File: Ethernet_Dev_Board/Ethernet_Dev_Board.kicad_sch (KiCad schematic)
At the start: 27 parts, among them J101 Power In, J102 5V, J103 3.3V, J104 3.3VA, J105 3.3VD, U101 AZ1117

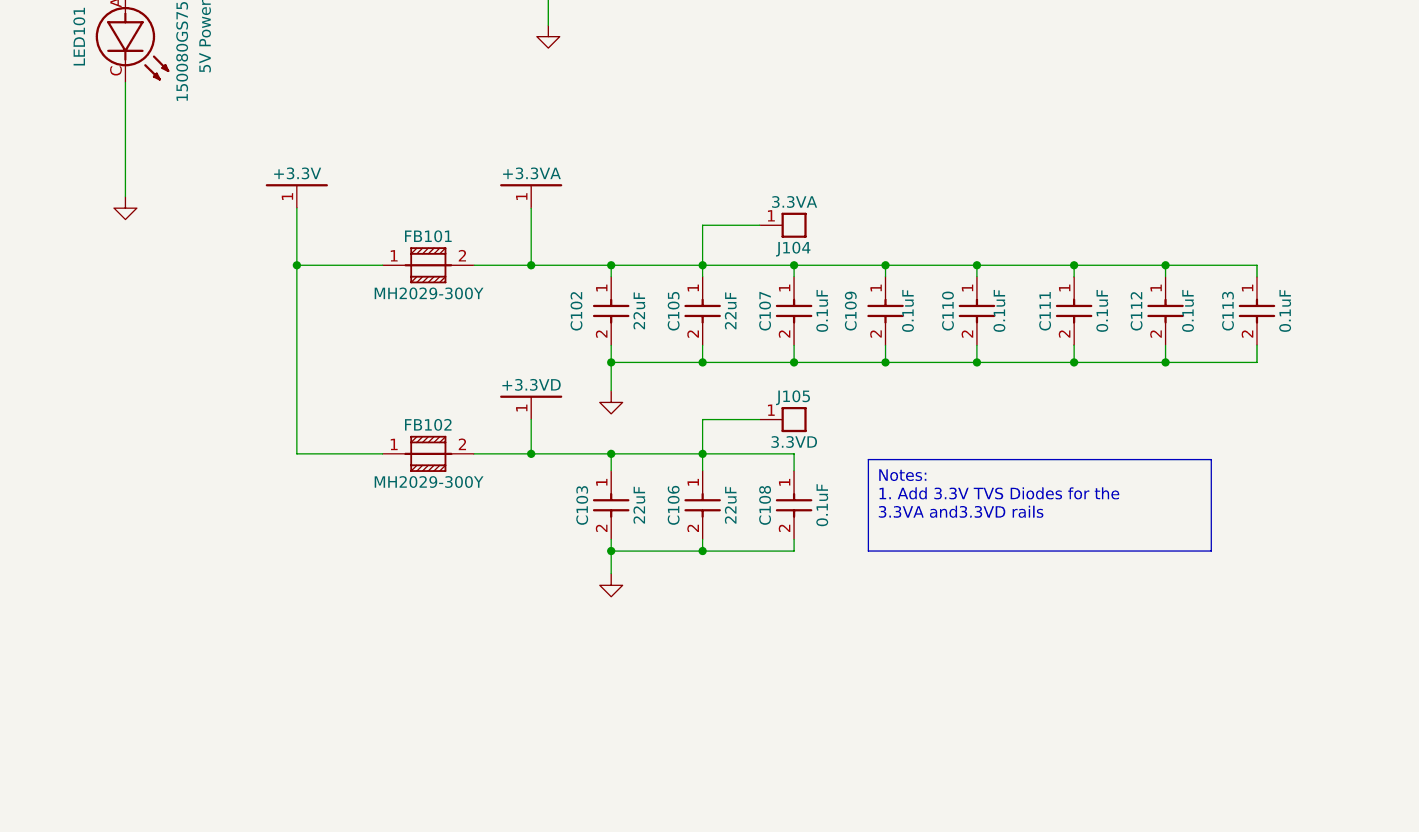
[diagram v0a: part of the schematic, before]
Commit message: Added TVS diode and redid the LED circuit on the ESP32
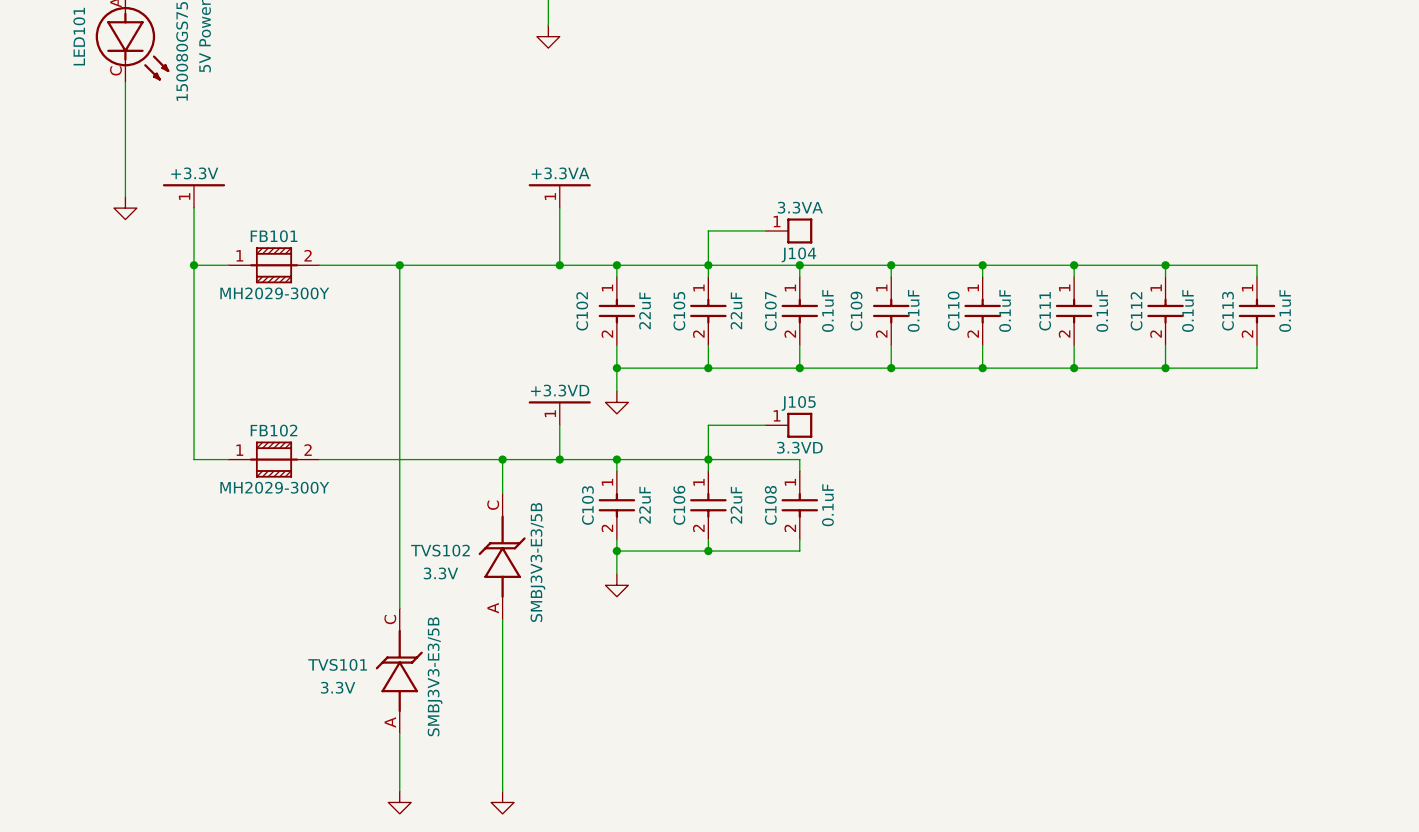
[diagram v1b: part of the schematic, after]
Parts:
- added TVS101, TVS102: 3.3V, RG_Diode:SMB-D, symbol RG_Diode:TVS
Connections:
- net +3.3VA: now also TVS101.C (2)
- net +3.3VD: now also TVS102.C (2)
- net GNDS: now also TVS101.A (1), TVS102.A (1)
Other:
- moved on the sheet: C102, C103, C105, C106, C107, C108, C109, C110, FB101, FB102, J104, J105

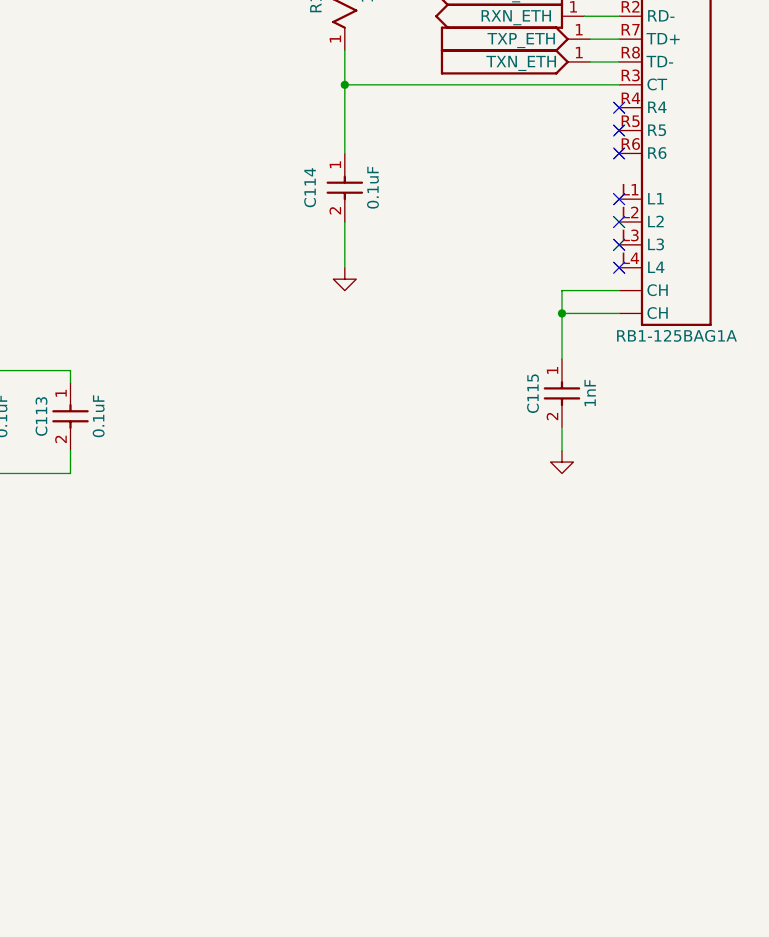
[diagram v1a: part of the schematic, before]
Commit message: Added in 1.2 V regulator and broke out unused IO pins to header
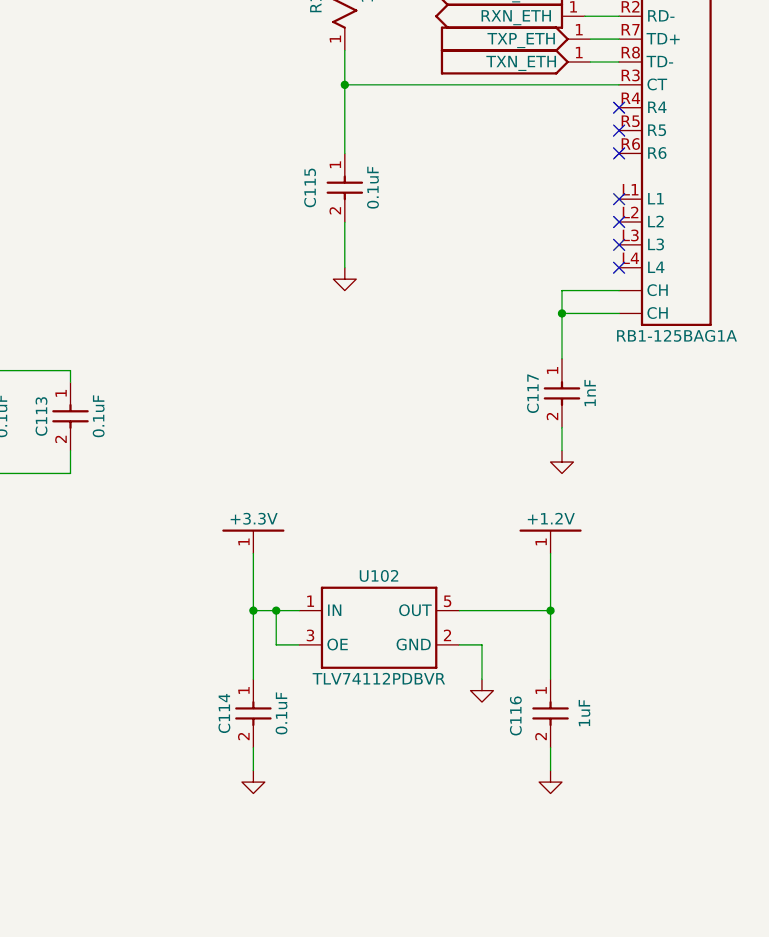
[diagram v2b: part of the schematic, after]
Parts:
- added C114: 0.1uF, RG_Capacitors_SMD:0603, symbol LED_Controller_Hardware-eagle-import:CAP-0603
- added C116: 1uF, RG_Capacitors_SMD:0603, symbol RG_Capacitors:CAP-0603
- added U102: 1.2V, RG_TO_SOT_SMD:SOT23-5P65, symbol RG_Regulators:TLV74112PDBVR
- renumbered C114 to C115, C115 to C117
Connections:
- net +3.3V: now also C114.1, U102.1 (IN), U102.3 (OE)
- net GNDS: now also C114.2, C116.2, U102.2 (GND)
- new net +1.2V: C116.1, U102.5 (OUT)

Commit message: Net adjustments. Beginning board layout
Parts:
- removed J102: 5V, RG_Terminals:PAD_0.0638, symbol LED_Controller_Hardware-eagle-import:5V
- removed J103: 3.3V, RG_Terminals:PAD_0.0638, symbol LED_Controller_Hardware-eagle-import:3.3V
- removed J104: 3.3VA, RG_Terminals:PAD_0.0638, symbol LED_Controller_Hardware-eagle-import:3.3VA
- removed J105: 3.3VD, RG_Terminals:PAD_0.0638, symbol LED_Controller_Hardware-eagle-import:3.3VD
- LED101: value 5V Power -> Power
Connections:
- net GND1: now also C102.2, C103.2, C105.2, C106.2, C107.2, C108.2, C109.2, C110.2, C111.2, C112.2, C113.2, C114.2, C115.2, C116.2, C117.2, TVS101.A (1), TVS102.A (1)
- net GNDS: no longer C102.2, C103.2, C105.2, C106.2, C107.2, C108.2, C109.2, C110.2, C111.2, C112.2, C113.2, C114.2, C115.2, C116.2, C117.2, TVS101.A (1), TVS102.A (1)
- net RXN_ETH renamed ETH_RX_N
- net RXP_ETH renamed ETH_RX_P
- net TXN_ETH renamed ETH_TX_N
- net TXP_ETH renamed ETH_TX_P

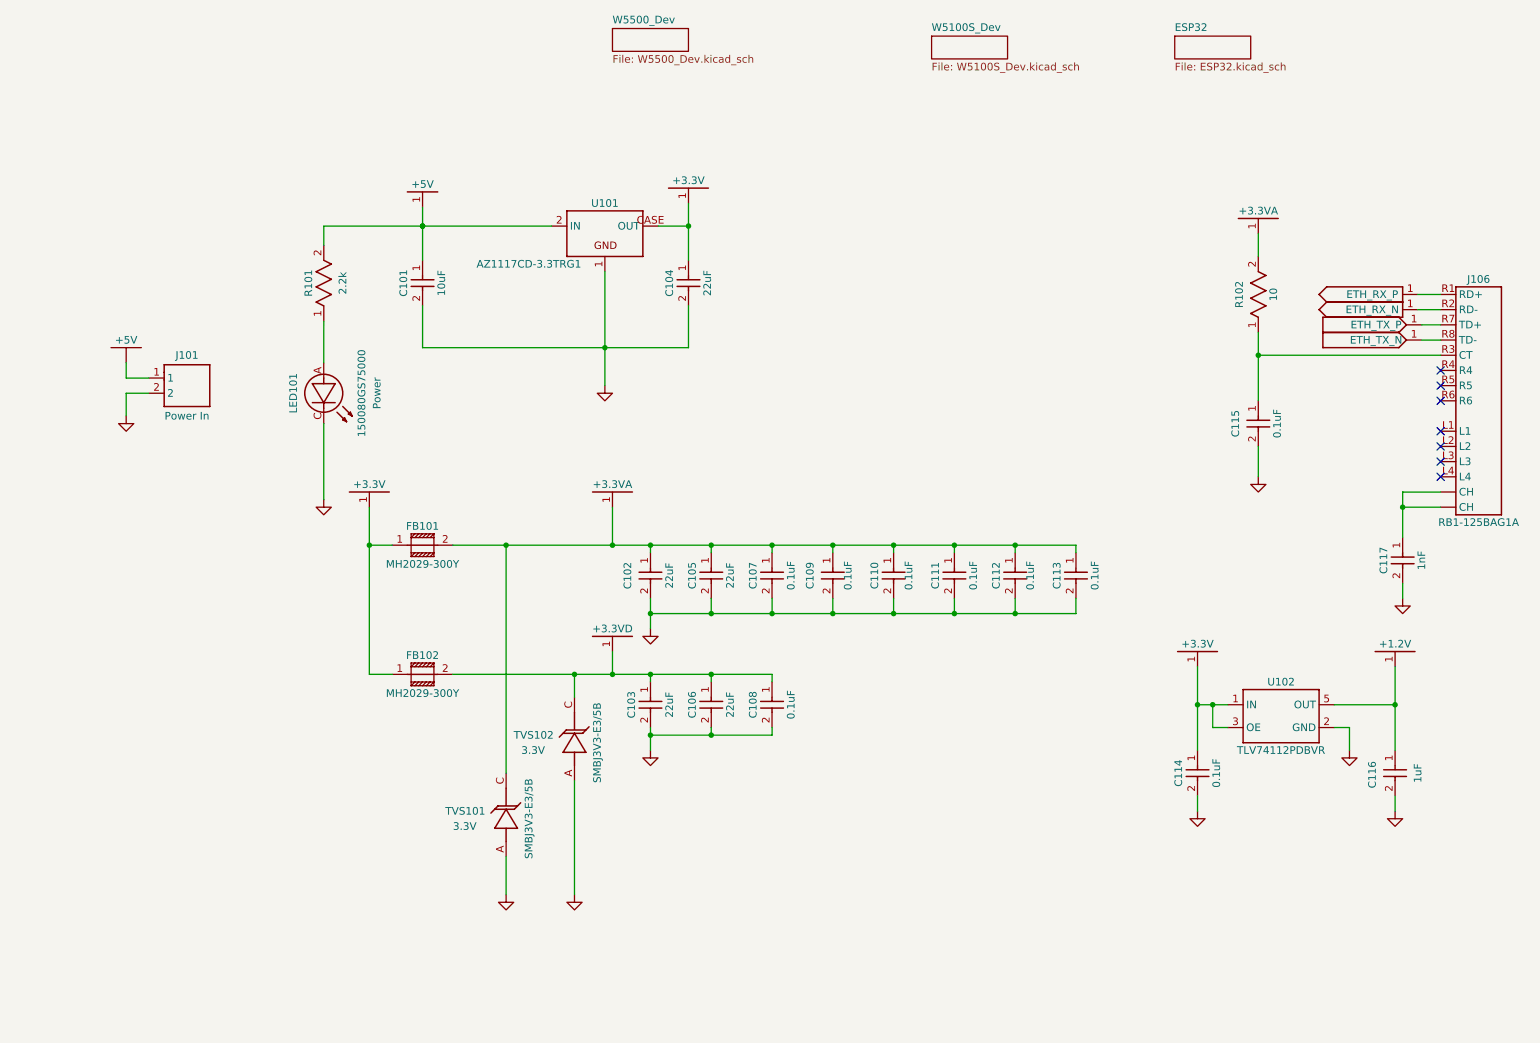
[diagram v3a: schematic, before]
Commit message: Removed 1 TVS diode. removed 1 reset circuit. Placed Ethernet port in both W5500 and W5100S circuits
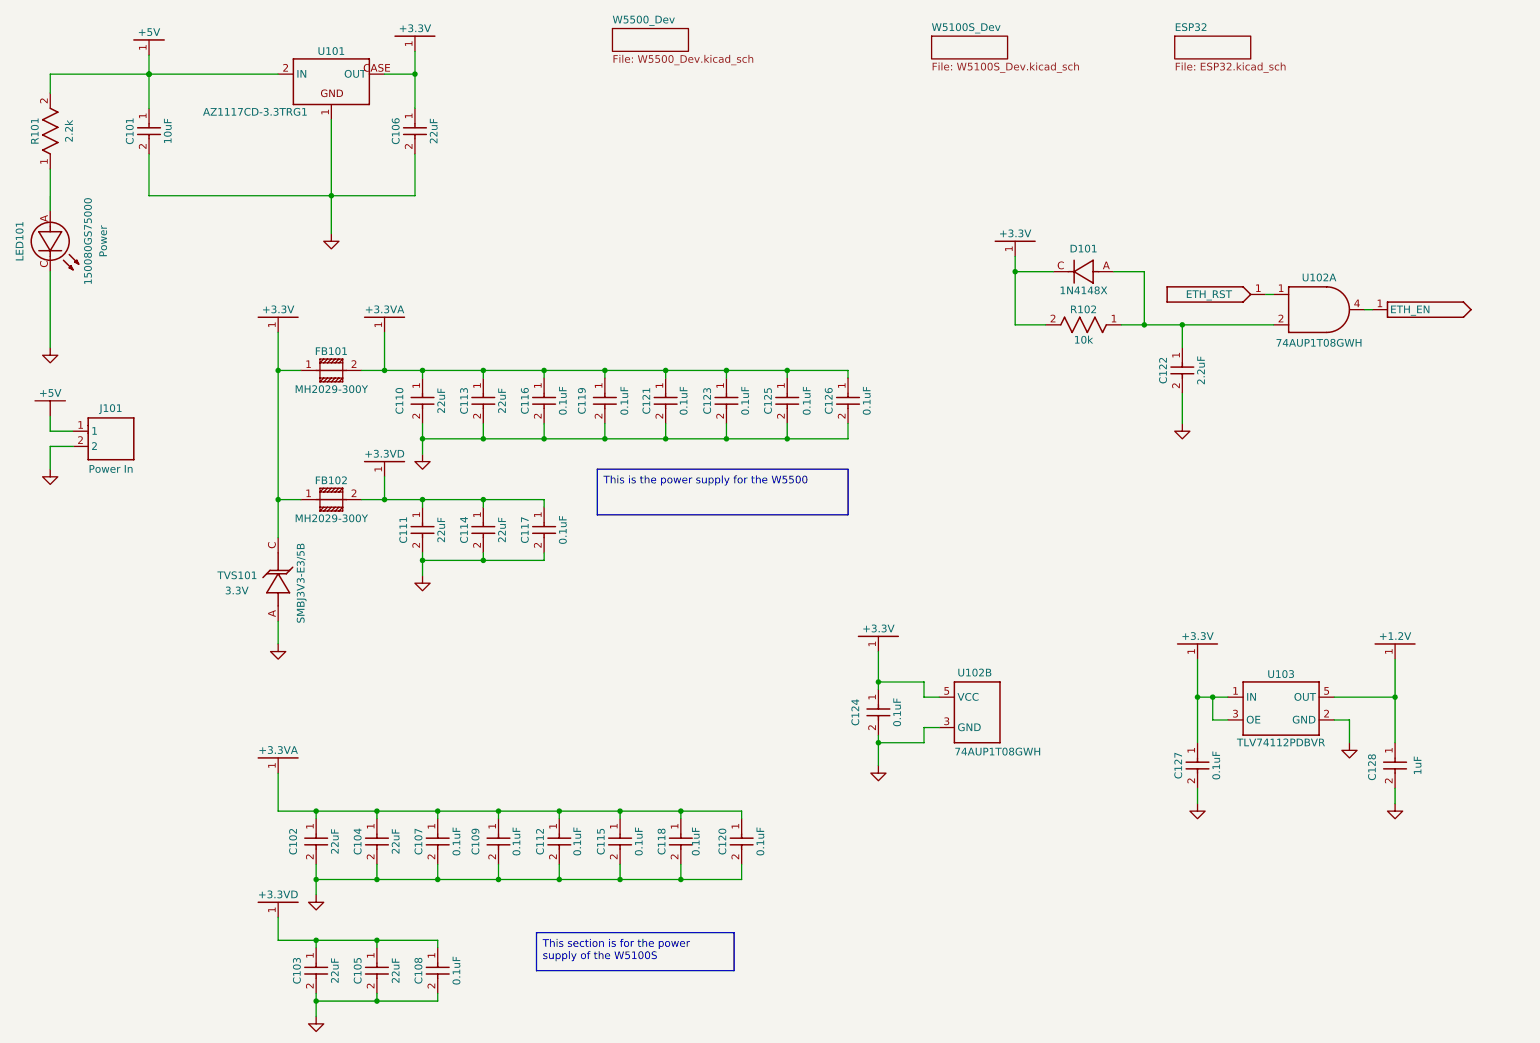
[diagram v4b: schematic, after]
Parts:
- removed C117: 1nF, RG_Capacitors_SMD:1206, symbol LED_Controller_Hardware-eagle-import:CAP-1206
- removed J106: ~, RG_Connectors:WIZNET_RB1-125BAG1A, symbol RG_Connectors:RB1-125BAG1A
- removed TVS102: 3.3V, RG_Diode:SMB-D, symbol RG_Diode:TVS
- added C102, C103, C104, C105: 22uF, RG_Capacitors_SMD:0603, symbol LED_Controller_Hardware-eagle-import:CAP-0603
- added C107, C108, C109, C112, C118, C120, C124: 0.1uF, RG_Capacitors_SMD:0603, symbol LED_Controller_Hardware-eagle-import:CAP-0603
- added C122: 2.2uF, RG_Capacitors_SMD:0603, symbol LED_Controller_Hardware-eagle-import:CAP-0603
- added D101: 1N4148X, RG_Diode:SOD-523-D, symbol LED_Controller_Hardware-eagle-import:1N4148X
- added U102: 74AUP1T08GWH, RG_TO_SOT_SMD:SOT23-5P65, symbol RG_Logic:74AUP1T08GWH
- R102: value 10 -> 10k; Distributor PN RMCF0603FT10R0TR-ND -> RMCF0603FT10K0TR-ND; Mfg. PN RMCF0603FT10R0 -> RMCF0603FT10K0
- renumbered C104 to C106, C102 to C110, C103 to C111, C105 to C113, C106 to C114, C107 to C116, C108 to C117, C109 to C119, C110 to C121, C111 to C123, C112 to C125, C113 to C126, C114 to C127, C116 to C128, U102 to U103
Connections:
- net +3.3V: now also R102.2, TVS101.C (2), C124.1, D101.C, U102.5 (VCC)
- net +3.3VA: now also C115.1, C102.1, C104.1, C107.1, C109.1, C112.1, C118.1, C120.1; no longer R102.2, TVS101.C (2)
- net +3.3VD: now also C103.1, C105.1, C108.1
- net GND1: now also C102.2, C103.2, C104.2, C105.2, C107.2, C108.2, C109.2, C112.2, C118.2, C120.2, C122.2, C124.2, U102.3 (GND)
- net at R102.1: now also C122.1, D101.A, U102.2 (C); no longer C115.1
- new net ETH_EN: U102.4 (Y)
- new net ETH_RST: U102.1 (A)
- no-connect marks 7 -> 0
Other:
- moved on the sheet: C101, C106, C110, C111, C113, C114, C116, C117, C119, C121, C123, C125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

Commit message: Removed unnecessary nets. Beginning board routing
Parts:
- removed C102, C103, C104, C105: 22uF, RG_Capacitors_SMD:0603, symbol LED_Controller_Hardware-eagle-import:CAP-0603
- removed C108, C112, C115, C120: 0.1uF, RG_Capacitors_SMD:0603, symbol LED_Controller_Hardware-eagle-import:CAP-0603
- added C116: 0.1uF, RG_Capacitors_SMD:0603, symbol LED_Controller_Hardware-eagle-import:CAP-0603
- added FB103: ~, RG_Resistors_SMD:0603, symbol RG_resistors:Ferrite_Bead_0603
- renumbered C110 to C107, C111 to C108, C107 to C109, C113 to C111, C114 to C112, C109 to C113, C116 to C114, C117 to C115, C119 to C117, C121 to C119, C123 to C121, C125 to C123, C126 to C124, C124 to C125, C122 to C126
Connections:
- net GNDS is gone; now on net GND1: U103.2 (GND)
- net +3.3V: now also C109.1, C113.1, FB103.1
- net +3.3VA: no longer C109.1, C113.1, C118.1
- net GND1: now also C116.2
- new net +3.3VA2: C116.1, C118.1, FB103.2
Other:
- moved on the sheet: C109, C113

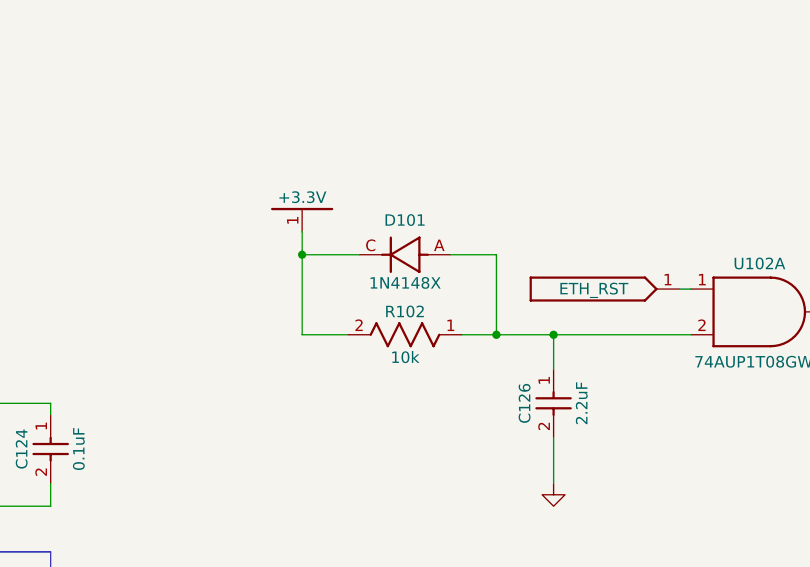
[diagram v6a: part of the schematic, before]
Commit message: Added ordering BOM for REV A
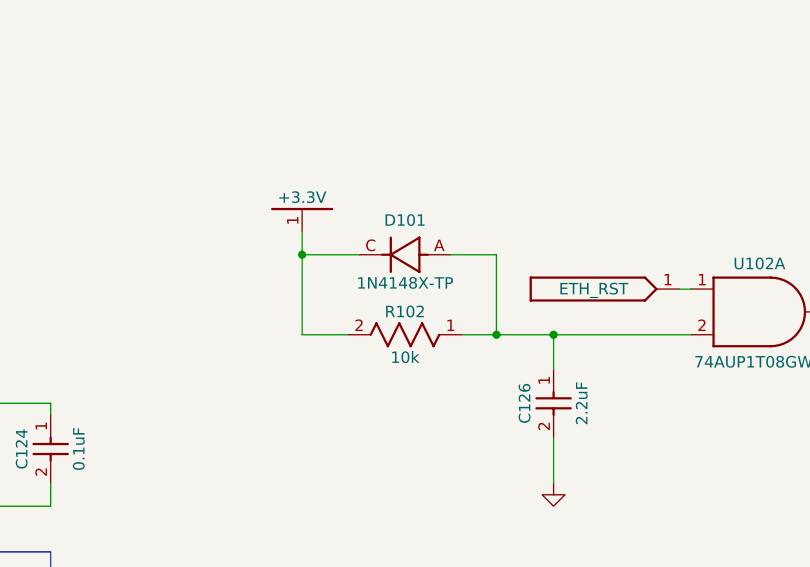
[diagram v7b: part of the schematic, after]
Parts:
- D101: Mfg. PN 1N4148X -> 1N4148X-TP
- J101: Distributor (none) -> Digikey; Distributor PN (none) -> 102-6406-ND; Mfg. (none) -> CUI Devices
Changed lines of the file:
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@@
 			)
 		)
-		(property "Datasheet" ""
+		(property "Datasheet" "https://www.cuidevices.com/product/resource/tbp01r1-508.pdf"
 			(at 36.83 88.9 0)
 			(effects
@@
 			)
 		)
-		(property "Mfg." ""
+		(property "Mfg." "CUI Devices"
 			(at 36.83 88.9 0)
 			(effects
@@
 			)
 		)
-		(property "Distributor" ""
+		(property "Distributor" "Digikey"
 			(at 36.83 88.9 0)
 			(effects
@@
 			)
 		)
-		(property "Distributor PN" ""
+		(property "Distributor PN" "102-6406-ND"
 			(at 36.83 88.9 0)
 			(effects
@@
 			)
 		)
-		(property "Description" "CAP-0603"
+		(property "Description" "CAP CER 2.2UF 10V X5R 0603"
 			(at 215.9 77.47 0)
 			(effects
@@
 			)
 		)
-		(property "Description" ""
+		(property "Description" "CAP-0603"
 			(at 251.46 143.51 0)
 			(effects
@@
 			)
 		)
-		(property "Mfg. PN" "1N4148X"
+		(property "Mfg. PN" "1N4148X-TP"
 			(at 199.39 64.135 0)
 			(effects
